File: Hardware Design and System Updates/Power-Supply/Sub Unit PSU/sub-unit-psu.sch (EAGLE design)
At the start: 3 parts, among them IC1 MCP1703CB

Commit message: Uploaded main and unit sch
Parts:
- removed G1: CRAA, battery:CRAA
- added B1: BK-18650-PC8BK-18650-PC8_MPD, 2023-03-07_13-29-57_Library:BK-18650-PC8BK-18650-PC8_MPD
- added D1, D2, D3: 1N4004, diode:1N4004
- DC1: MF MURATA POWER SOLUTIONS -> (none); MPN CME0303S3C -> (none); OC_NEWARK 29X1501 -> (none)
- IC1: value MCP1703CB -> V-REG_MCP1700T/MB; device linear:MCP1703CB -> 52101-101-REV-A_v16:V-REG_MCP1700T/MB; OC_NEWARK unknown -> (none)
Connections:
- new net N$1: IC1.OUT
- new net N$2: B1.4, B1.6
- new net N$3: D2.C, D3.A
- new net N$5: D1.C, D2.A
- new net N$8: B1.3, D1.A
- net 0: now also B1.5; no longer G1.-
- net N$4: now also IC1.IN; no longer IC1.VI
- net N$6: now also D3.C; no longer G1.+

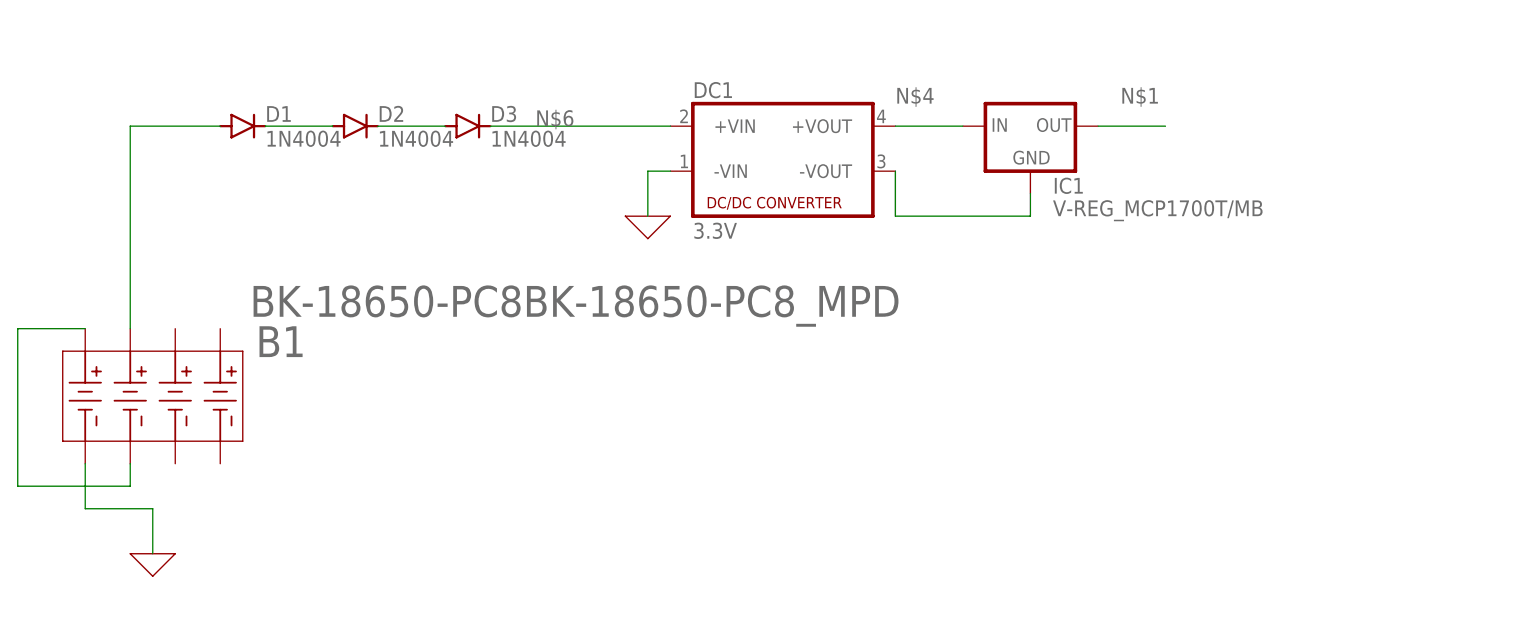
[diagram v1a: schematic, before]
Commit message: Fixed main and sub unit psu sch
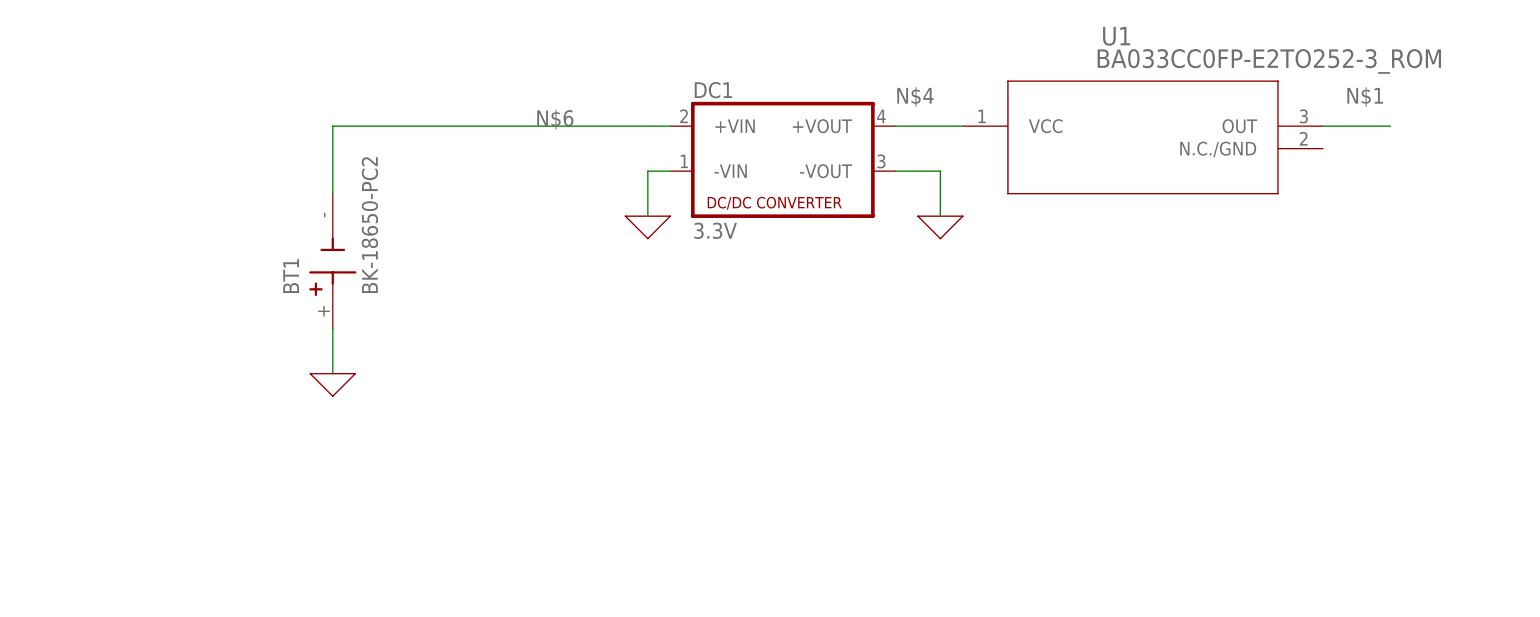
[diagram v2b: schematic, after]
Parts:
- removed B1: BK-18650-PC8BK-18650-PC8_MPD, 2023-03-07_13-29-57_Library:BK-18650-PC8BK-18650-PC8_MPD
- removed D1, D2, D3: 1N4004, diode:1N4004
- removed IC1: V-REG_MCP1700T/MB, 52101-101-REV-A_v16:V-REG_MCP1700T/MB
- added BT1: BK-18650-PC2, BK-18650-PC2:BK-18650-PC2
- added U1: BA033CC0FP-E2TO252-3_ROM, 2023-03-08_12-17-23_Library:BA033CC0FP-E2TO252-3_ROM
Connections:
- removed net N$2: B1.4, B1.6
- removed net N$3: D2.C, D3.A
- removed net N$5: D1.C, D2.A
- removed net N$7: DC1.-VOUT, IC1.GND
- removed net N$8: B1.3, D1.A
- net 0: now also BT1.+, DC1.-VOUT; no longer B1.5
- net N$1: now also U1.OUT; no longer IC1.OUT
- net N$4: now also U1.VCC; no longer IC1.IN
- net N$6: now also BT1.-; no longer D3.C
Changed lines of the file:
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@@
 </classes>
 <parts>
-<part name="X_5" library="ngspice-simulation" library_urn="urn:adsk.eagle:library:527439" deviceset="GND" device=""/>
 <part name="DC1" library="dc-dc-converter" library_urn="urn:adsk.eagle:library:208" deviceset="NME" device="" package3d_urn="urn:adsk.eagle:package:12313/1" value="3.3V"/>
 <part name="X_4" library="ngspice-simulation" library_urn="urn:adsk.eagle:library:527439" deviceset="GND" device=""/>
-<part name="IC1" library="52101-101-REV-A_v16" library_urn="urn:adsk.eagle:library:21899384" deviceset="V-REG_MCP1700T/MB" device="" package3d_urn="urn:adsk.eagle:package:15662289/2"/>
-<part name="B1" library="2023-03-07_13-29-57_Library" deviceset="BK-18650-PC8" device="BK-18650-PC8_MPD"/>
-<part name="D1" library="diode" library_urn="urn:adsk.eagle:library:210" deviceset="1N4004" device="" package3d_urn="urn:adsk.eagle:package:43336/1"/>
-<part name="D2" library="diode" library_urn="urn:adsk.eagle:library:210" deviceset="1N4004" device="" package3d_urn="urn:adsk.eagle:package:43336/1"/>
-<part name="D3" library="diode" library_urn="urn:adsk.eagle:library:210" deviceset="1N4004" device="" package3d_urn="urn:adsk.eagle:package:43336/1"/>
+<part name="BT1" library="BK-18650-PC2" deviceset="BK-18650-PC2" device=""/>
+<part name="X_1" library="ngspice-simulation" library_urn="urn:adsk.eagle:library:527439" deviceset="GND" device=""/>
+<part name="U1" library="2023-03-08_12-17-23_Library" deviceset="BA033CC0FP-E2" device="TO252-3_ROM"/>
+<part name="X_2" library="ngspice-simulation" library_urn="urn:adsk.eagle:library:527439" deviceset="GND" device=""/>
 </parts>
 <sheets>
@@
 </plain>
 <instances>
-<instance part="X_5" gate="G$1" x="96.52" y="101.6" smashed="yes"/>
 <instance part="DC1" gate="G$1" x="167.64" y="147.32" smashed="yes">
 <attribute name="NAME" x="157.48" y="153.035" size="1.778" layer="95"/>
@@
 </instance>
 <instance part="X_4" gate="G$1" x="152.4" y="139.7" smashed="yes"/>
-<instance part="IC1" gate="G$1" x="195.58" y="149.86" smashed="yes">
-<attribute name="NAME" x="198.12" y="142.24" size="1.778" layer="95"/>
-<attribute name="VALUE" x="198.12" y="139.7" size="1.778" layer="96"/>
+<instance part="BT1" gate="G$1" x="116.84" y="134.62" smashed="yes" rot="R90">
+<attribute name="NAME" x="113.03" y="130.81" size="1.778" layer="95" rot="R90"/>
+<attribute name="VALUE" x="121.92" y="130.81" size="1.778" layer="96" rot="R90"/>
 </instance>
-<instance part="B1" gate="A" x="104.14" y="127" smashed="yes" rot="R270">
-<attribute name="NAME" x="113.8301" y="127.2748" size="3.48" layer="95" ratio="10" rot="R180"/>
-<attribute name="VALUE" x="107.4801" y="128.3431" size="3.48" layer="96" ratio="10"/>
+<instance part="X_1" gate="G$1" x="116.84" y="121.92" smashed="yes"/>
+<instance part="U1" gate="A" x="185.42" y="149.86" smashed="yes">
+<attribute name="NAME" x="203.5546" y="158.9786" size="2.083" layer="95" ratio="6"/>
+<attribute name="VALUE" x="202.9152" y="156.4386" size="2.083" layer="96" ratio="6"/>
 </instance>
-<instance part="D1" gate="1" x="106.68" y="149.86" smashed="yes">
-<attribute name="NAME" x="109.22" y="150.3426" size="1.778" layer="95"/>
-<attribute name="VALUE" x="109.22" y="147.5486" size="1.778" layer="96"/>
-</instance>
-<instance part="D2" gate="1" x="119.38" y="149.86" smashed="yes">
-<attribute name="NAME" x="121.92" y="150.3426" size="1.778" layer="95"/>
-<attribute name="VALUE" x="121.92" y="147.5486" size="1.778" layer="96"/>
-</instance>
-<instance part="D3" gate="1" x="132.08" y="149.86" smashed="yes">
-<attribute name="NAME" x="134.62" y="150.3426" size="1.778" layer="95"/>
-<attribute name="VALUE" x="134.62" y="147.5486" size="1.778" layer="96"/>
-</instance>
+<instance part="X_2" gate="G$1" x="185.42" y="139.7" smashed="yes"/>
 </instances>
 <busses>
@@
 <net name="0" class="0">
 <segment>
-<pinref part="X_5" gate="G$1" pin="0"/>
-<wire x1="96.52" y1="101.6" x2="96.52" y2="106.68" width="0.1524" layer="91"/>
-<wire x1="96.52" y1="106.68" x2="88.9" y2="106.68" width="0.1524" layer="91"/>
-<pinref part="B1" gate="A" pin="5"/>
-<wire x1="88.9" y1="106.68" x2="88.9" y2="111.76" width="0.1524" layer="91"/>
-</segment>
-<segment>
 <pinref part="X_4" gate="G$1" pin="0"/>
 <pinref part="DC1" gate="G$1" pin="-VIN"/>
@@
 <wire x1="152.4" y1="144.78" x2="154.94" y2="144.78" width="0.1524" layer="91"/>
 </segment>
-</net>
-<net name="N$6" class="0">
 <segment>
-<pinref part="DC1" gate="G$1" pin="+VIN"/>
-<wire x1="134.62" y1="149.86" x2="154.94" y2="149.86" width="0.1524" layer="91"/>
-<label x="139.7" y="149.86" size="1.778" layer="95"/>
-<pinref part="D3" gate="1" pin="C"/>
+<pinref part="X_1" gate="G$1" pin="0"/>
+<pinref part="BT1" gate="G$1" pin="+"/>
+<wire x1="116.84" y1="121.92" x2="116.84" y2="127" width="0.1524" layer="91"/>
+</segment>
+<segment>
+<pinref part="DC1" gate="G$1" pin="-VOUT"/>
+<wire x1="180.34" y1="144.78" x2="185.42" y2="144.78" width="0.1524" layer="91"/>
+<wire x1="185.42" y1="144.78" x2="185.42" y2="139.7" width="0.1524" layer="91"/>
+<pinref part="X_2" gate="G$1" pin="0"/>
 </segment>
 </net>
@@
 <wire x1="180.34" y1="149.86" x2="187.96" y2="149.86" width="0.1524" layer="91"/>
 <label x="180.34" y="152.4" size="1.778" layer="95"/>
-<pinref part="IC1" gate="G$1" pin="IN"/>
-</segment>
-</net>
-<net name="N$7" class="0">
-<segment>
-<pinref part="DC1" gate="G$1" pin="-VOUT"/>
-<wire x1="180.34" y1="144.78" x2="180.34" y2="139.7" width="0.1524" layer="91"/>
-<wire x1="180.34" y1="139.7" x2="195.58" y2="139.7" width="0.1524" layer="91"/>
-<wire x1="195.58" y1="139.7" x2="195.58" y2="142.24" width="0.1524" layer="91"/>
-<pinref part="IC1" gate="G$1" pin="GND"/>
+<pinref part="U1" gate="A" pin="VCC"/>
 </segment>
 </net>
 <net name="N$1" class="0">
 <segment>
-<wire x1="203.2" y1="149.86" x2="210.82" y2="149.86" width="0.1524" layer="91"/>
-<label x="205.74" y="152.4" size="1.778" layer="95"/>
-<pinref part="IC1" gate="G$1" pin="OUT"/>
+<wire x1="228.6" y1="149.86" x2="236.22" y2="149.86" width="0.1524" layer="91"/>
+<label x="231.14" y="152.4" size="1.778" layer="95"/>
+<pinref part="U1" gate="A" pin="OUT"/>
 </segment>
 </net>
-<net name="N$2" class="0">
+<net name="N$6" class="0">
 <segment>
-<pinref part="B1" gate="A" pin="4"/>
-<wire x1="88.9" y1="127" x2="81.28" y2="127" width="0.1524" layer="91"/>
-<wire x1="81.28" y1="127" x2="81.28" y2="109.22" width="0.1524" layer="91"/>
-<pinref part="B1" gate="A" pin="6"/>
-<wire x1="81.28" y1="109.22" x2="93.98" y2="109.22" width="0.1524" layer="91"/>
-<wire x1="93.98" y1="109.22" x2="93.98" y2="111.76" width="0.1524" layer="91"/>
+<pinref part="BT1" gate="G$1" pin="-"/>
+<wire x1="116.84" y1="142.24" x2="116.84" y2="149.86" width="0.1524" layer="91"/>
+<pinref part="DC1" gate="G$1" pin="+VIN"/>
+<wire x1="116.84" y1="149.86" x2="154.94" y2="149.86" width="0.1524" layer="91"/>
+<label x="139.7" y="149.86" size="1.778" layer="95"/>
 </segment>
 </net>
-<net name="N$3" class="0">
-<segment>
-<pinref part="D3" gate="1" pin="A"/>
-<pinref part="D2" gate="1" pin="C"/>
-<wire x1="121.92" y1="149.86" x2="129.54" y2="149.86" width="0.1524" layer="91"/>
-</segment>
-</net>
-<net name="N$5" class="0">
-<segment>
-<pinref part="D2" gate="1" pin="A"/>
-<pinref part="D1" gate="1" pin="C"/>
-<wire x1="109.22" y1="149.86" x2="116.84" y2="149.86" width="0.1524" layer="91"/>
-</segment>
-</net>
-<net name="N$8" class="0">
-<segment>
-<pinref part="B1" gate="A" pin="3"/>
-<wire x1="93.98" y1="127" x2="93.98" y2="149.86" width="0.1524" layer="91"/>
-<wire x1="93.98" y1="149.86" x2="104.14" y2="149.86" width="0.1524" layer="91"/>
-<pinref part="D1" gate="1" pin="A"/>
-</segment>
-</net>

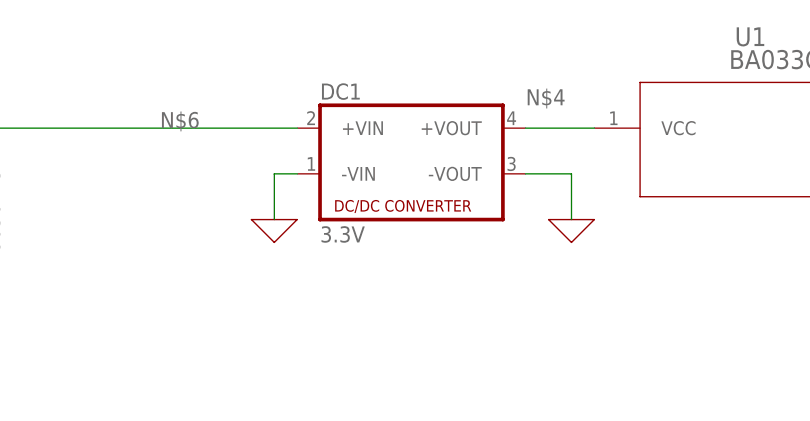
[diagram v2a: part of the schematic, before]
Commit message: Fixed 3.3 regulator and BOM
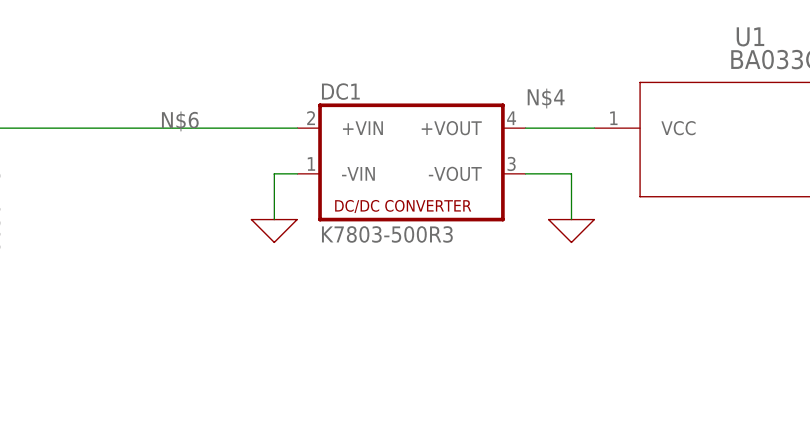
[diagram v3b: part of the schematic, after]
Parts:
- DC1: value 3.3V -> K7803-500R3
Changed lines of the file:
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@@
 </classes>
 <parts>
-<part name="DC1" library="dc-dc-converter" library_urn="urn:adsk.eagle:library:208" deviceset="NME" device="" package3d_urn="urn:adsk.eagle:package:12313/1" value="3.3V"/>
+<part name="DC1" library="dc-dc-converter" library_urn="urn:adsk.eagle:library:208" deviceset="NME" device="" package3d_urn="urn:adsk.eagle:package:12313/1" value="K7803-500R3"/>
 <part name="X_4" library="ngspice-simulation" library_urn="urn:adsk.eagle:library:527439" deviceset="GND" device=""/>
 <part name="BT1" library="BK-18650-PC2" deviceset="BK-18650-PC2" device=""/>

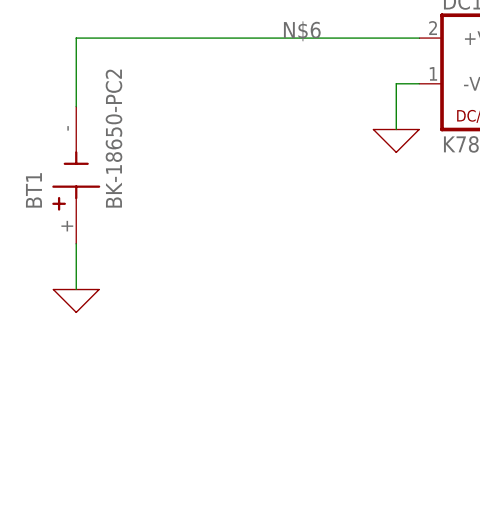
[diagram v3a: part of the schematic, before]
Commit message: Fixed main and sub unit designs for voltage compat
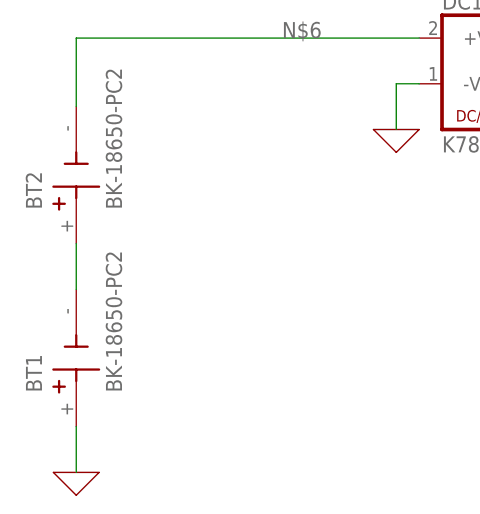
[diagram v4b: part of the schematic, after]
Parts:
- added BT2: BK-18650-PC2, BK-18650-PC2:BK-18650-PC2
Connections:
- new net N$2: BT1.-, BT2.+
- net N$6: now also BT2.-; no longer BT1.-
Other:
- moved on the sheet: BT1
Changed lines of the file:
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@@
 <part name="U1" library="2023-03-08_12-17-23_Library" deviceset="BA033CC0FP-E2" device="TO252-3_ROM"/>
 <part name="X_2" library="ngspice-simulation" library_urn="urn:adsk.eagle:library:527439" deviceset="GND" device=""/>
+<part name="BT2" library="BK-18650-PC2" deviceset="BK-18650-PC2" device=""/>
 </parts>
 <sheets>
@@
 </instance>
 <instance part="X_4" gate="G$1" x="152.4" y="139.7" smashed="yes"/>
-<instance part="BT1" gate="G$1" x="116.84" y="134.62" smashed="yes" rot="R90">
-<attribute name="NAME" x="113.03" y="130.81" size="1.778" layer="95" rot="R90"/>
-<attribute name="VALUE" x="121.92" y="130.81" size="1.778" layer="96" rot="R90"/>
+<instance part="BT1" gate="G$1" x="116.84" y="114.3" smashed="yes" rot="R90">
+<attribute name="NAME" x="113.03" y="110.49" size="1.778" layer="95" rot="R90"/>
+<attribute name="VALUE" x="121.92" y="110.49" size="1.778" layer="96" rot="R90"/>
 </instance>
-<instance part="X_1" gate="G$1" x="116.84" y="121.92" smashed="yes"/>
+<instance part="X_1" gate="G$1" x="116.84" y="101.6" smashed="yes"/>
 <instance part="U1" gate="A" x="185.42" y="149.86" smashed="yes">
 <attribute name="NAME" x="203.5546" y="158.9786" size="2.083" layer="95" ratio="6"/>
@@
 </instance>
 <instance part="X_2" gate="G$1" x="185.42" y="139.7" smashed="yes"/>
+<instance part="BT2" gate="G$1" x="116.84" y="134.62" smashed="yes" rot="R90">
+<attribute name="NAME" x="113.03" y="130.81" size="1.778" layer="95" rot="R90"/>
+<attribute name="VALUE" x="121.92" y="130.81" size="1.778" layer="96" rot="R90"/>
+</instance>
 </instances>
 <busses>
@@
 <pinref part="X_1" gate="G$1" pin="0"/>
 <pinref part="BT1" gate="G$1" pin="+"/>
-<wire x1="116.84" y1="121.92" x2="116.84" y2="127" width="0.1524" layer="91"/>
+<wire x1="116.84" y1="101.6" x2="116.84" y2="106.68" width="0.1524" layer="91"/>
 </segment>
 <segment>
@@
 <net name="N$6" class="0">
 <segment>
-<pinref part="BT1" gate="G$1" pin="-"/>
-<wire x1="116.84" y1="142.24" x2="116.84" y2="149.86" width="0.1524" layer="91"/>
 <pinref part="DC1" gate="G$1" pin="+VIN"/>
 <wire x1="116.84" y1="149.86" x2="154.94" y2="149.86" width="0.1524" layer="91"/>
 <label x="139.7" y="149.86" size="1.778" layer="95"/>
+<pinref part="BT2" gate="G$1" pin="-"/>
+<wire x1="116.84" y1="142.24" x2="116.84" y2="149.86" width="0.1524" layer="91"/>
 </segment>
 </net>
+<net name="N$2" class="0">
+<segment>
+<pinref part="BT1" gate="G$1" pin="-"/>
+<pinref part="BT2" gate="G$1" pin="+"/>
+<wire x1="116.84" y1="127" x2="116.84" y2="121.92" width="0.1524" layer="91"/>
+</segment>
+</net>

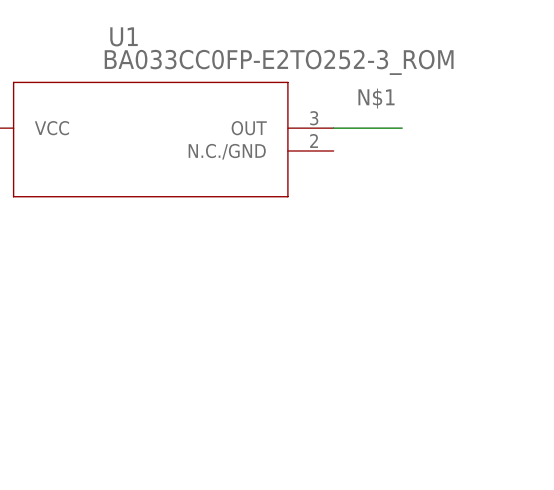
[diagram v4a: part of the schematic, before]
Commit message: Finished BOM,analysis and diagrams for PSUs
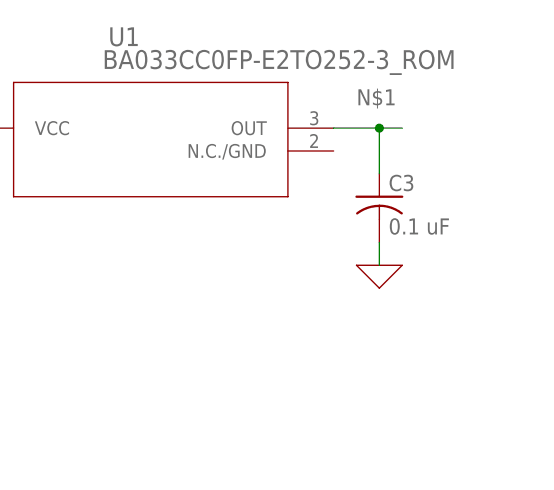
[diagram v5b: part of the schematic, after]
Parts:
- added C3: 0.1 uF, rcl:C-US050-024X044
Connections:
- net 0: now also C3.2
- net N$1: now also C3.1
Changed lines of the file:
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@@
 <part name="X_2" library="ngspice-simulation" library_urn="urn:adsk.eagle:library:527439" deviceset="GND" device=""/>
 <part name="BT2" library="BK-18650-PC2" deviceset="BK-18650-PC2" device=""/>
+<part name="C3" library="rcl" library_urn="urn:adsk.eagle:library:334" deviceset="C-US" device="050-024X044" package3d_urn="urn:adsk.eagle:package:23643/1" value="0.1 uF"/>
+<part name="X_10" library="ngspice-simulation" library_urn="urn:adsk.eagle:library:527439" deviceset="GND" device=""/>
 </parts>
 <sheets>
@@
 <attribute name="VALUE" x="121.92" y="130.81" size="1.778" layer="96" rot="R90"/>
 </instance>
+<instance part="C3" gate="G$1" x="233.68" y="142.24" smashed="yes">
+<attribute name="NAME" x="234.696" y="142.875" size="1.778" layer="95"/>
+<attribute name="VALUE" x="234.696" y="138.049" size="1.778" layer="96"/>
+</instance>
+<instance part="X_10" gate="G$1" x="233.68" y="134.62" smashed="yes"/>
 </instances>
 <busses>
@@
 <pinref part="X_2" gate="G$1" pin="0"/>
 </segment>
+<segment>
+<pinref part="X_10" gate="G$1" pin="0"/>
+<pinref part="C3" gate="G$1" pin="2"/>
+<wire x1="233.68" y1="134.62" x2="233.68" y2="137.16" width="0.1524" layer="91"/>
+</segment>
 </net>
 <net name="N$4" class="0">
@@
 <net name="N$1" class="0">
 <segment>
-<wire x1="228.6" y1="149.86" x2="236.22" y2="149.86" width="0.1524" layer="91"/>
+<wire x1="228.6" y1="149.86" x2="233.68" y2="149.86" width="0.1524" layer="91"/>
 <label x="231.14" y="152.4" size="1.778" layer="95"/>
 <pinref part="U1" gate="A" pin="OUT"/>
+<pinref part="C3" gate="G$1" pin="1"/>
+<wire x1="233.68" y1="149.86" x2="236.22" y2="149.86" width="0.1524" layer="91"/>
+<wire x1="233.68" y1="144.78" x2="233.68" y2="149.86" width="0.1524" layer="91"/>
+<junction x="233.68" y="149.86"/>
 </segment>
 </net>
